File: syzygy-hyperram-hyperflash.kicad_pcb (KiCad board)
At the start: 4 copper layers, 45 x 70 mm, 37 parts, among them IC1 ATTINY44A-MMH, IC2 TLV6710DDCT, IC3 S27KL0641DABHI020, IC4 S71KL256SC0BHI, J1 SYZYGY_STD, J2 Conn_02x03_Odd_Even, J3 Conn_02x03_Odd_Even

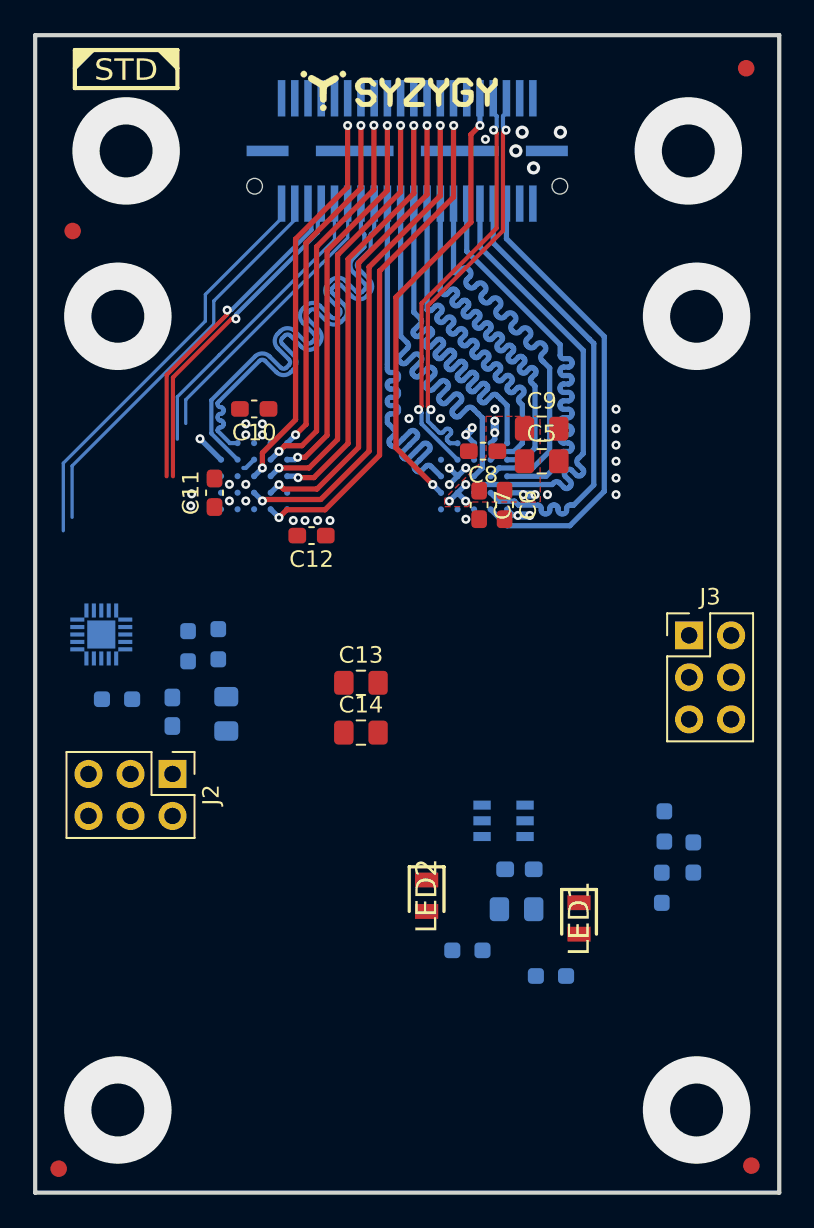
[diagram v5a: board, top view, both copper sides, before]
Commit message: Finished routing HyperFlash with equalized trace length
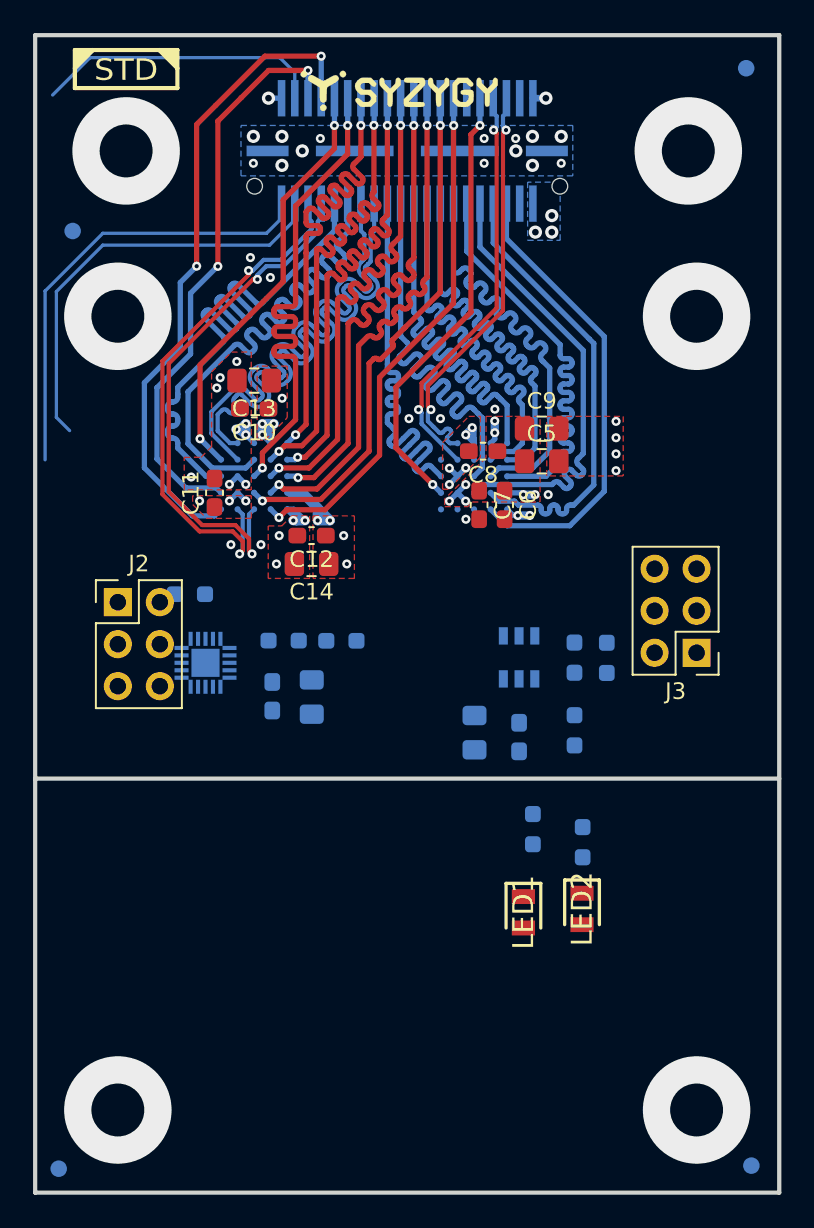
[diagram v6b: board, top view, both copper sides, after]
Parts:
- FID5, FID6, FID7, FID8: moved to B.Cu
- moved C13 19.4 mm to (114.9, 74.2), turned to 180 degrees
- moved R5 14.1 mm to (134.2, 91.0)
- moved C3 11.0 mm to (128.2, 95.5), turned to -90 degrees
- moved J2 10.9 mm to (106.6, 87.6), turned to 0 degrees
- moved R6 10.9 mm to (134.2, 95.4)
- moved R4 10.8 mm to (136.2, 91.0), turned to 90 degrees
- moved C14 10.6 mm to (118.3, 85.3), turned to 180 degrees
- moved IC2 9.93 mm to (130.9, 90.9), turned to -90 degrees
- moved R3 9.56 mm to (134.7, 102.1), turned to 90 degrees
- moved LED2 9.43 mm to (134.7, 106.2)
- moved R7 9.28 mm to (120.1, 89.9), turned to 180 degrees
- moved R2 8.95 mm to (131.7, 101.3), turned to 90 degrees
- moved C4 8.00 mm to (130.9, 95.8), turned to -90 degrees
- moved R1 7.73 mm to (111.0, 87.1)
- moved IC1 6.53 mm to (111.9, 91.3), turned to -90 degrees
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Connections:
- J1 pad 10: /HF_RSTN -> /HF_RSTON
- J1 pad 11: /HF_CS2N -> /HF_CSN
- J1 pad 6: /HF_RSTON -> /HF_RSTN
- J1 pad 9: /HF_CSN -> /HF_CS2N
- LED1 pad 1: /VIO_UV -> Net-(LED1-Pad1)
- LED1 pad 2: Net-(LED1-Pad2) -> +3.3V
- LED2 pad 1: /VIO_OV -> Net-(LED2-Pad1)
- LED2 pad 2: Net-(LED2-Pad2) -> +3.3V
- R2 pad 1: +3.3V -> Net-(LED1-Pad1)
- R2 pad 2: Net-(LED1-Pad2) -> /VIO_UV
- R3 pad 1: +3.3V -> Net-(LED2-Pad1)
- R3 pad 2: Net-(LED2-Pad2) -> /VIO_OV
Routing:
- net /HF_INTN: track 0.00 -> 39.9 mm, vias 1 -> 2
- net /HF_RSTN: track 0.00 -> 35.1 mm, vias 1 -> 2
- net /HF_RSTON: track 1.79 -> 25.8 mm, vias 1 -> 2
- net /RGA: track 0.00 -> 17.5 mm
- net /HF_CS2N: track 17.4 -> 34.6 mm
- net /HF_CSN: track 19.0 -> 34.5 mm
- net VCC: track 5.30 -> 17.0 mm, vias 13 -> 21
- net /HF_PSC+: track 20.4 -> 31.9 mm, vias 1 -> 2
- net /HF_PSC-: track 20.4 -> 31.9 mm, vias 1 -> 2
- net /HF_DQ7: track 21.1 -> 31.7 mm
- net GND: track 4.90 -> 14.5 mm, vias 29 -> 47
- net /HF_DQ6: track 23.3 -> 31.6 mm
- net /HF_DQ1: track 23.4 -> 31.7 mm
- net /HF_RWDS: track 23.6 -> 31.7 mm
- net /HF_DQ5: track 25.5 -> 31.7 mm
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- added copper zone on B.Cu, net GND
- added copper zone on F.Cu, net GND
- added copper zone on B.Cu, net VCC
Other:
- outline, holes or cut-outs redrawn

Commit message: Removed unnecessary holes to make pcb smaller. Rearranged signals connected to ATTiny.
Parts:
- moved C3 25.8 mm to (143.9, 75.1), turned to 90 degrees
- moved C4 23.2 mm to (141.2, 75.0), turned to 90 degrees
- moved J3 20.6 mm to (138.6, 70.3), turned to 90 degrees
- moved R6 20.4 mm to (138.3, 75.4), turned to 90 degrees
- moved R3 19.8 mm to (144.0, 84.7)
- moved LED1 18.5 mm to (140.9, 90.7)
- moved LED2 18.0 mm to (144.0, 90.7)
- moved R2 17.6 mm to (141.1, 86.4)
- moved IC2 15.4 mm to (141.2, 79.5), turned to 90 degrees
- moved R5 12.3 mm to (138.3, 79.4), turned to 90 degrees
- moved R4 8.01 mm to (138.3, 83.2)
- moved R7 2.86 mm to (118.8, 87.4)
- moved J2 2.26 mm to (104.8, 86.2)
- moved R8 1.76 mm to (116.0, 88.3), turned to -90 degrees
- moved C1 1.37 mm to (116.0, 91.9), turned to 90 degrees
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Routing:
- net /SCK: track 27.2 -> 12.1 mm
- net /SDA_MOSI: track 25.9 -> 13.2 mm
- net (no net): vias 6 -> 2

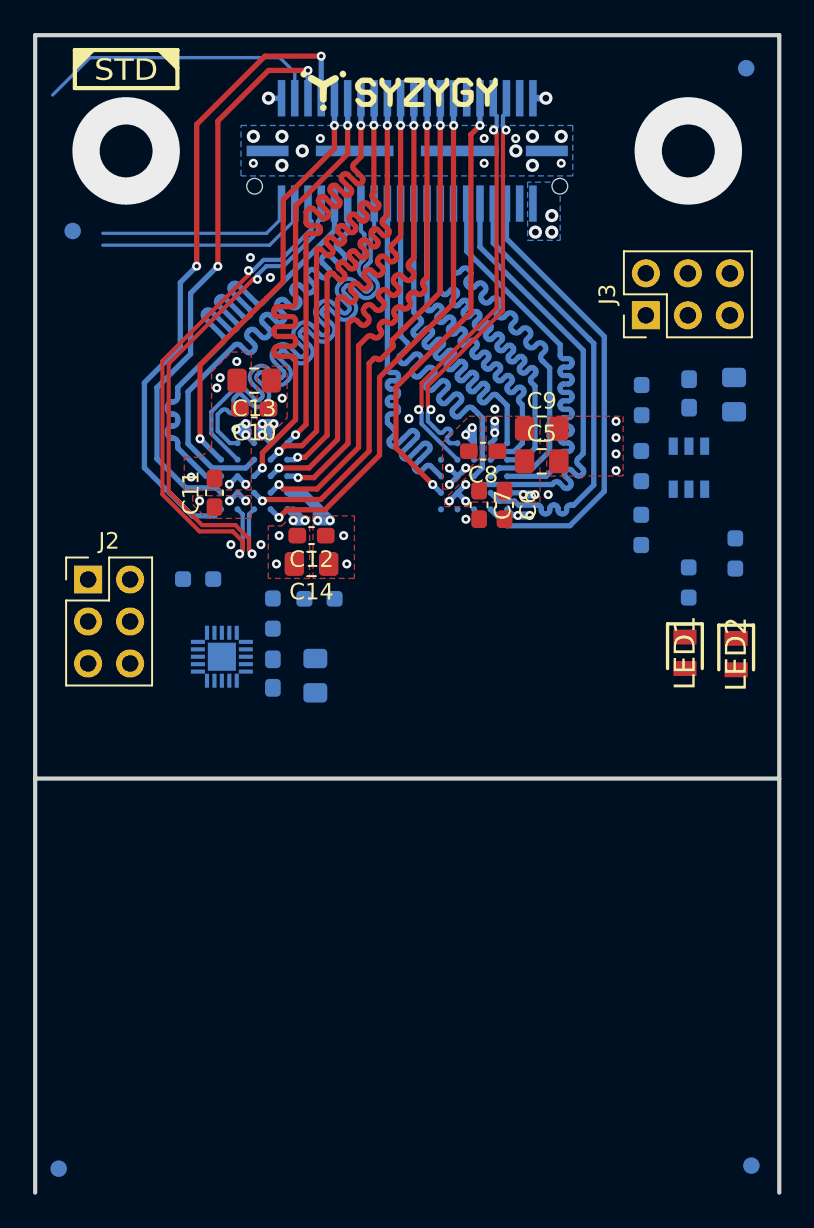
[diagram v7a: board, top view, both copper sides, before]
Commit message: Make PCB smaller, by reaaranging signals and footprints. First try of routing ATTiny.
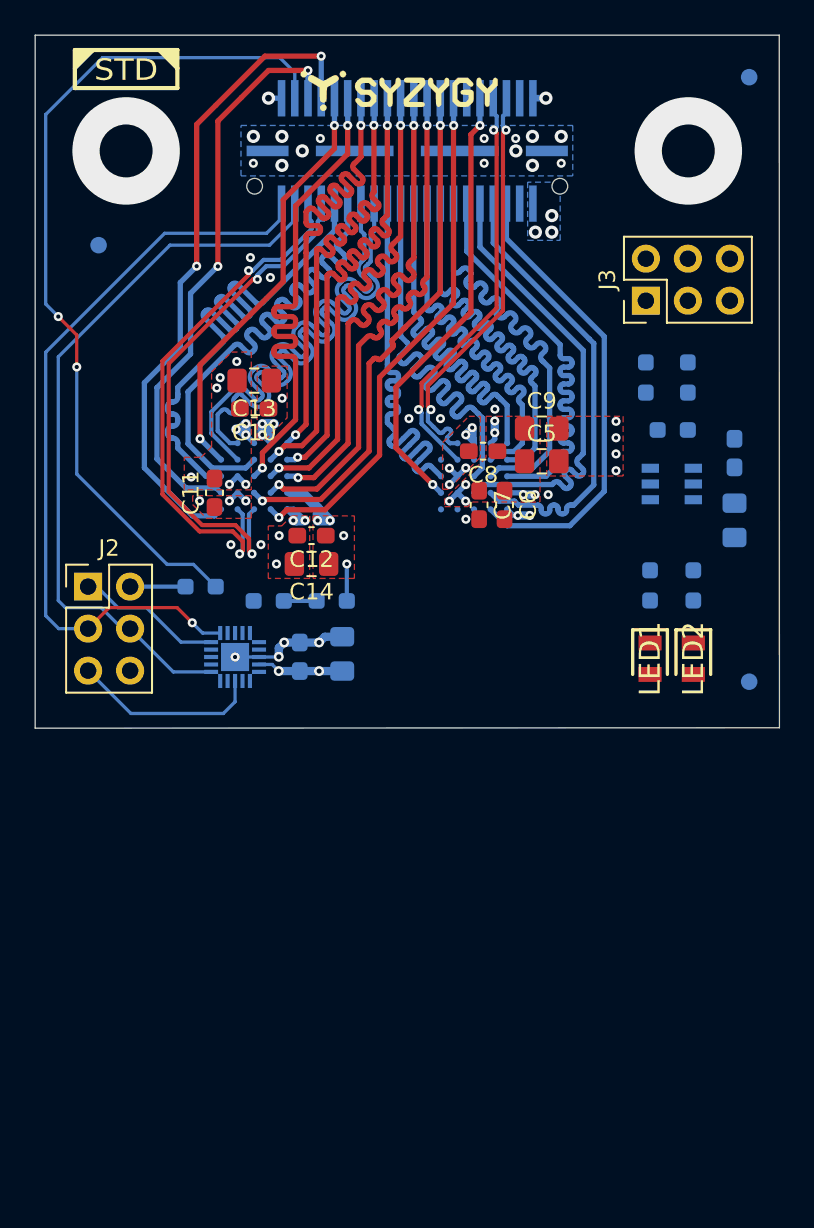
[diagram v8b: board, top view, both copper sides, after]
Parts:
- removed FID7: Fiducial, Fiducial:Fiducial_1mm_Mask2mm
- moved FID8 29.3 mm to (144.8, 92.4)
- moved R4 9.22 mm to (138.6, 74.0), turned to -90 degrees
- moved C3 7.60 mm to (143.9, 82.7), turned to -90 degrees
- moved C4 4.53 mm to (143.9, 78.6)
- moved R3 3.19 mm to (141.4, 86.6)
- moved R6 3.11 mm to (141.1, 74.0)
- moved R5 2.90 mm to (140.2, 77.2), turned to 0 degrees
- moved LED2 2.61 mm to (141.4, 91.0)
- moved R2 2.34 mm to (138.8, 86.6)
- moved LED1 2.14 mm to (138.8, 91.0)
- moved C2 2.09 mm to (120.2, 90.7)
- moved C1 1.92 mm to (117.6, 90.9)
- moved FID5 1.79 mm to (105.5, 66.0)
- moved IC2 1.43 mm to (140.1, 80.5), turned to 0 degrees
- moved J3 0.88 mm to (138.6, 69.4)
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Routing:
- net /RGA: track 17.5 -> 52.2 mm, vias 0 -> 2
- net /SCK: track 12.1 -> 46.5 mm, vias 0 -> 1
- net /SDA_MOSI: track 13.2 -> 44.5 mm
- net /nRESET: track 0.00 -> 11.5 mm
- net /MISO: track 0.00 -> 8.83 mm
- net +3.3V: track 0.79 -> 9.34 mm, vias 1 -> 3
- net GND: track 14.5 -> 21.8 mm, vias 47 -> 51
- net VCC: track 17.0 -> 19.3 mm
- net /VIO_sense: track 0.00 -> 1.98 mm
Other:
- board size 45 x 70 mm -> 45 x 41.9 mm
